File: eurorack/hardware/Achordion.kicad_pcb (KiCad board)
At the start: 4 copper layers, 44.5 x 109.4 mm, 120 parts, among them J1 Power, J10 Jack, J11 Jack, J2 Serial, J3 SWD, J4 Jack, J5 Jack, J6 Jack, J7 Jack, J8 Jack, J9 Jack, SW2 Button, U1 STM32F405RGT6, U10 SC39-11SURKWA, U2 LM1117-3.3, U3 LM1117-3.3, U4 LM4040C10, U5 TLV320AIC23BPW, U6 TL072, U7 MCP6002, U8 MCP6002, U9 MCP6002, Y1 8MHz

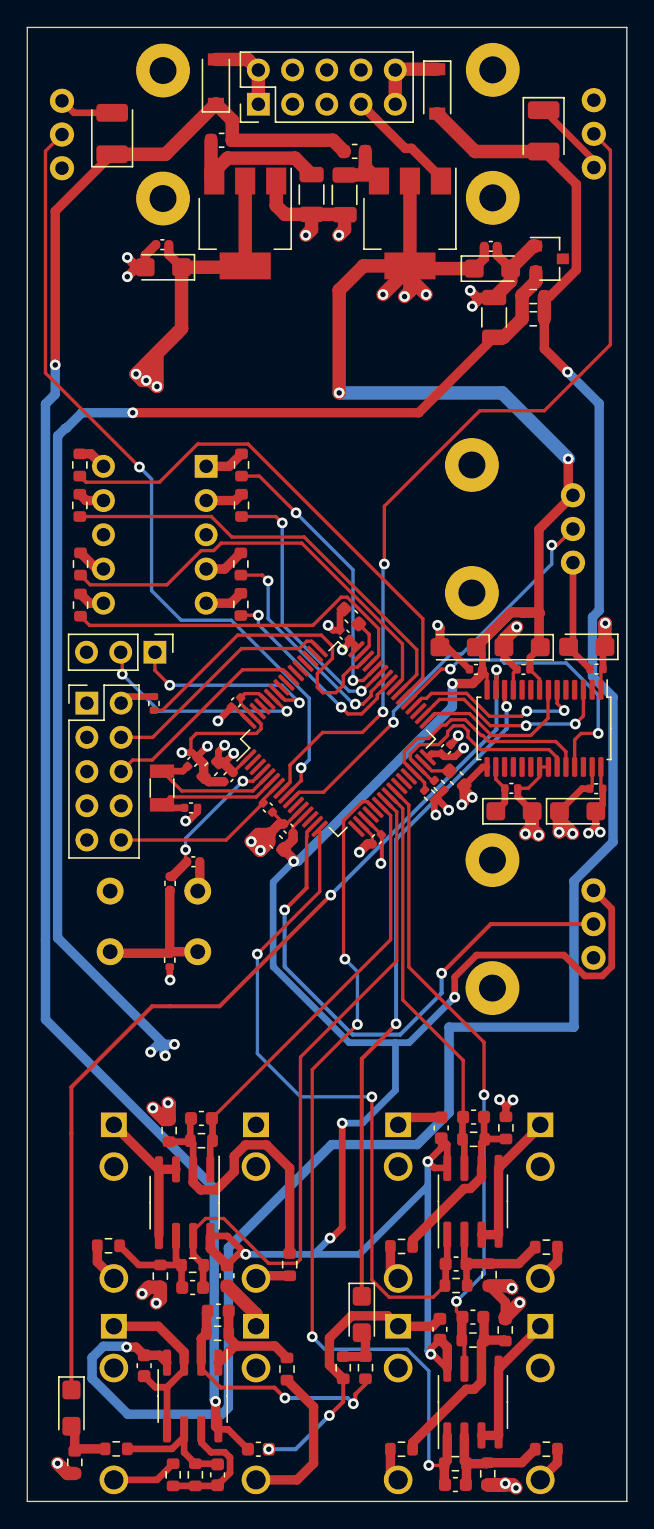
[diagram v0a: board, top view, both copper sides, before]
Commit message: Add labels to PCB
Signed-off-by: Petr Horacek <hrck@protonmail.com>
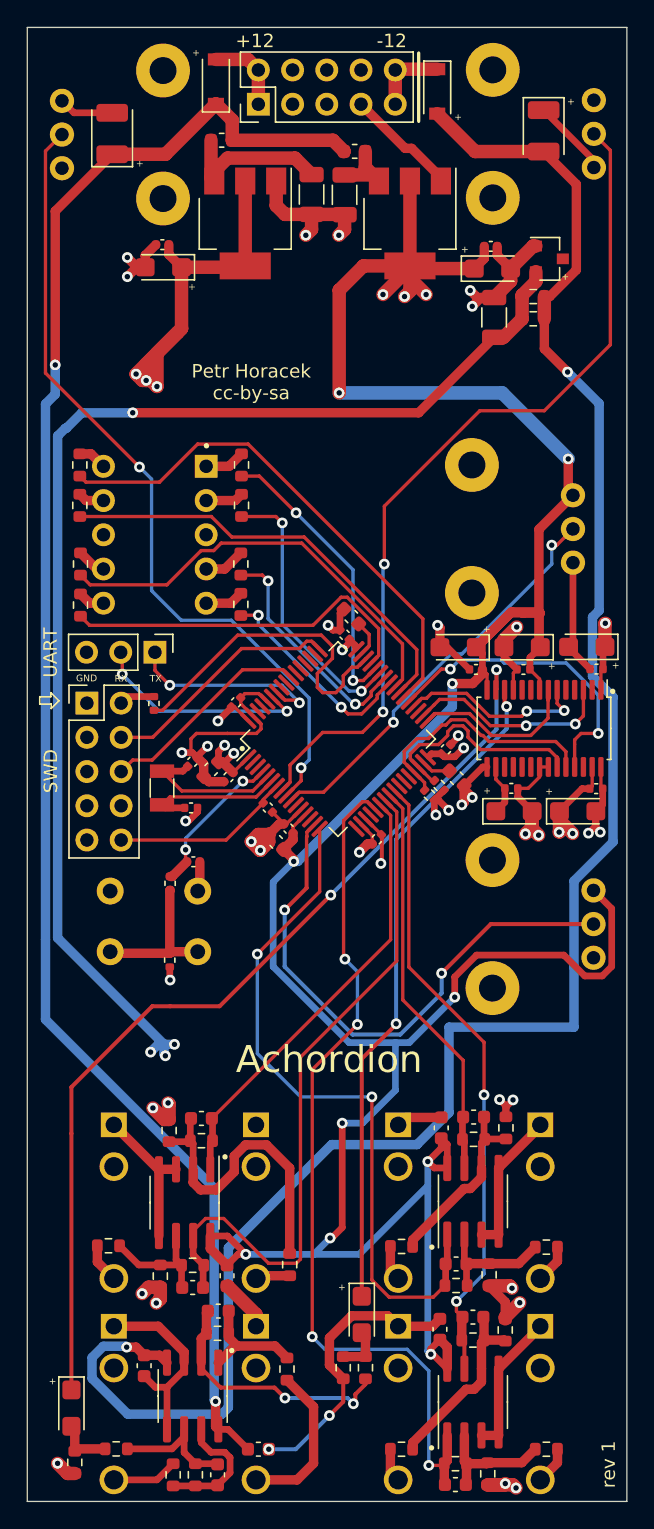
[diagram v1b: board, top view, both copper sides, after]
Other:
- board text added: "+"
- board text added: "+12"
- board text added: "-12"
- board text added: "Achordion"
- board text added: "GND"
- board text added: "Petr Horacek cc-by-sa"
- board text added: "RX"
- board text added: "SWD"
- board text added: "TX"
- board text added: "UART"
- board text added: "rev 1"

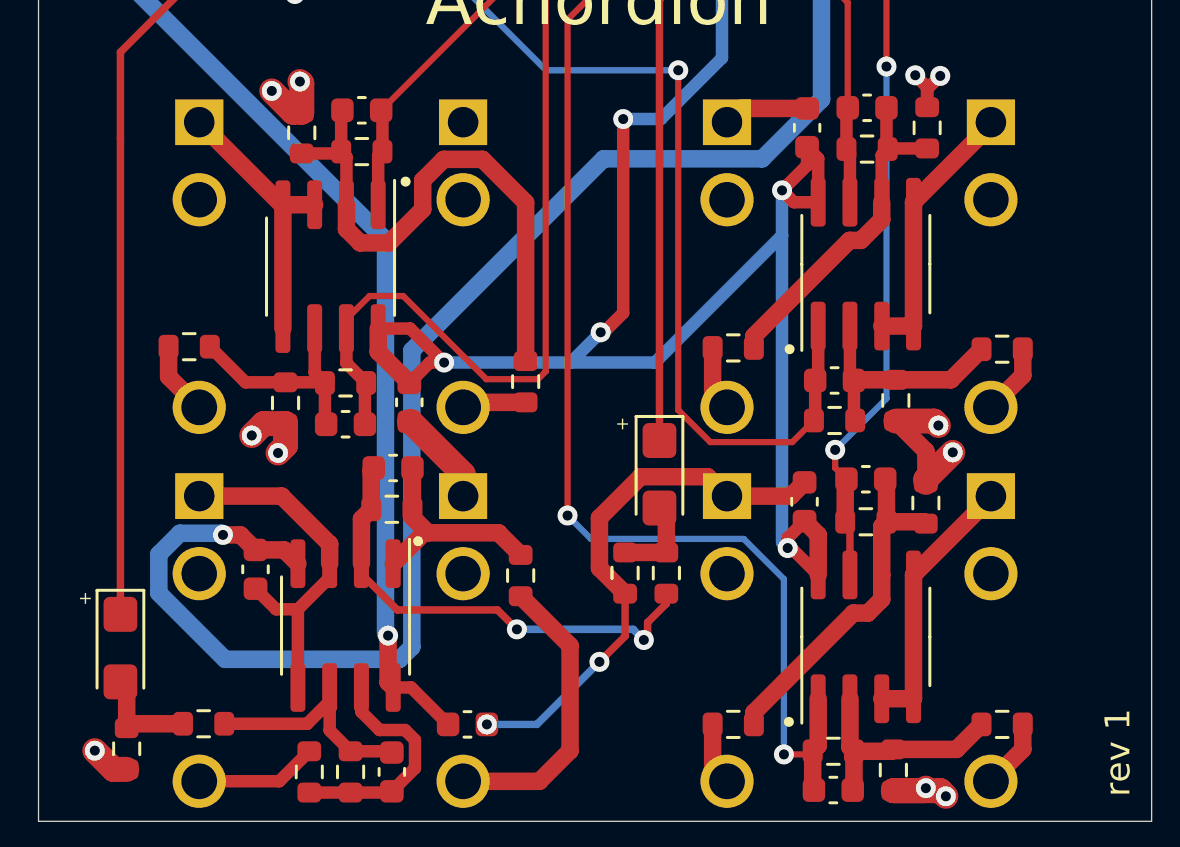
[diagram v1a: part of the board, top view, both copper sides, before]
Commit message: Cut out holes below jacks
Signed-off-by: Petr Horacek <hrck@protonmail.com>
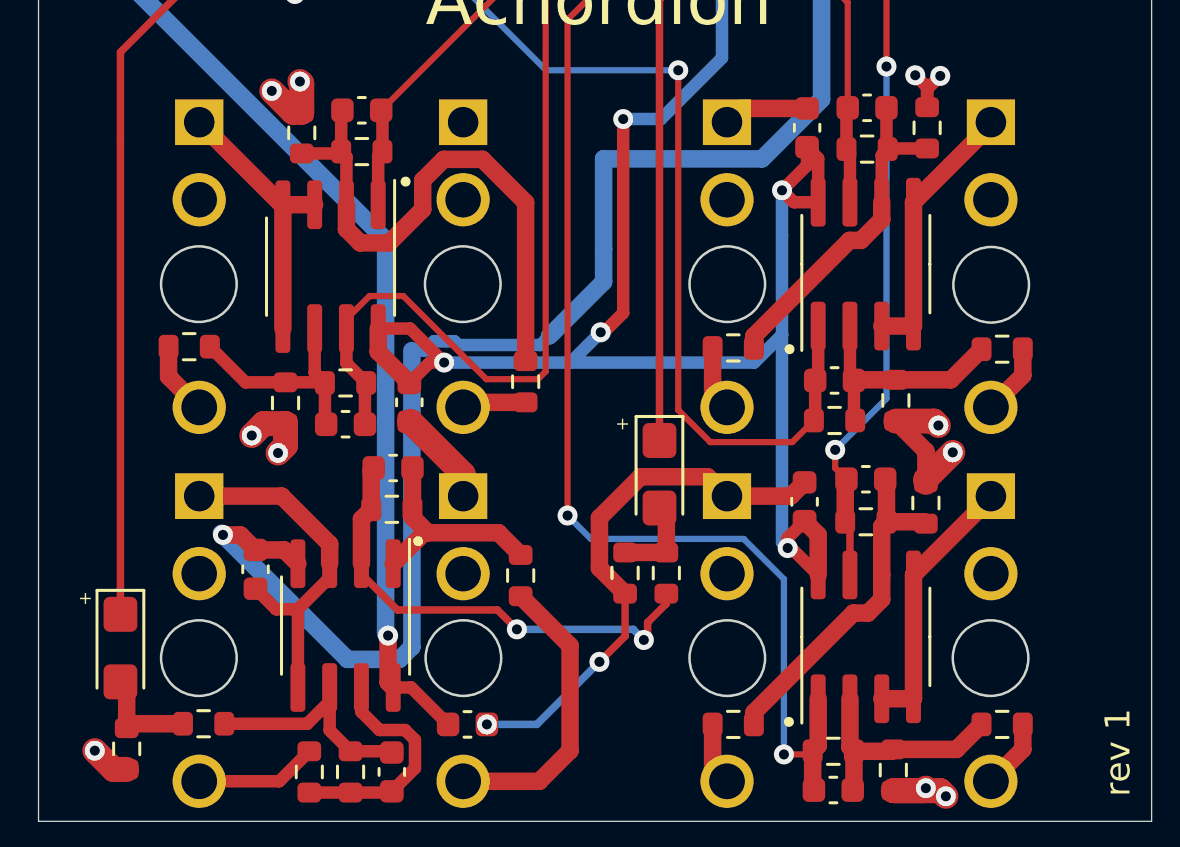
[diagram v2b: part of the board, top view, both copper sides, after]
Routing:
- net VEE: track 147.4 -> 144.4 mm
- net +3.3VA: track 231.3 -> 229.6 mm
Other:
- outline, holes or cut-outs redrawn
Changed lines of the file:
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@@
   (general
     (thickness 1.6)
-    (drawings 43)
-    (tracks 1046)
+    (drawings 51)
+    (tracks 1053)
     (zones 0)
     (modules 120)
@@
     (1 In1.Cu power hide)
     (2 In2.Cu power hide)
-    (31 B.Cu signal hide)
+    (31 B.Cu signal)
     (32 B.Adhes user)
     (33 F.Adhes user)
@@
   )
   (setup
-    (last_trace_width 0.25)
+    (last_trace_width 0.7)
     (user_trace_width 0.3)
     (user_trace_width 0.5)
@@
     )
   )
+  (gr_circle (center 129.236001 144.45) (end 130.747002 144.45) (layer Edge.Cuts) (width 0.1))
+  (gr_circle (center 139.811001 144.45) (end 141.322002 144.45) (layer Edge.Cuts) (width 0.1))
+  (gr_circle (center 150.361001 144.45) (end 151.872002 144.45) (layer Edge.Cuts) (width 0.1))
+  (gr_circle (center 160.886001 144.45) (end 162.397002 144.45) (layer Edge.Cuts) (width 0.1))
+  (gr_circle (center 160.911001 129.525) (end 162.422002 129.525) (layer Edge.Cuts) (width 0.1))
+  (gr_circle (center 150.361001 129.5) (end 151.872002 129.5) (layer Edge.Cuts) (width 0.1))
+  (gr_circle (center 129.236001 129.5) (end 130.747002 129.5) (layer Edge.Cuts) (width 0.1))
+  (gr_circle (center 139.786001 129.5) (end 141.297002 129.5) (layer Edge.Cuts) (width 0.1))
   (gr_text + (at 135.05 60.825) (layer F.SilkS)
     (effects (font (size 0.5 0.5) (thickness 0.125)))
@@
   (segment (start 152.775 140.05) (end 152.92 140.05) (width 0.5) (layer F.Cu) (net 5))
   (via (at 139.040948 132.634052) (size 0.8) (drill 0.4) (layers F.Cu B.Cu) (net 5))
-  (segment (start 152.55 127.55) (end 147.465948 132.634052) (width 0.5) (layer B.Cu) (net 5))
   (segment (start 152.55 125.75) (end 152.55 127.55) (width 0.5) (layer B.Cu) (net 5))
-  (segment (start 152.55 127.55) (end 152.55 139.825) (width 0.5) (layer B.Cu) (net 5))
   (segment (start 138.465948 132.634052) (end 137.65 133.45) (width 0.5) (layer F.Cu) (net 5))
   (segment (start 139.040948 132.634052) (end 138.465948 132.634052) (width 0.5) (layer F.Cu) (net 5))
@@
   (segment (start 143.984052 132.634052) (end 139.040948 132.634052) (width 0.5) (layer B.Cu) (net 5))
   (segment (start 145.3 131.425) (end 144.090948 132.634052) (width 0.5) (layer B.Cu) (net 5))
-  (segment (start 147.465948 132.634052) (end 143.984052 132.634052) (width 0.5) (layer B.Cu) (net 5))
+  (segment (start 151.440948 132.634052) (end 152.55 131.525) (width 0.5) (layer B.Cu) (net 5))
+  (segment (start 143.984052 132.634052) (end 151.440948 132.634052) (width 0.5) (layer B.Cu) (net 5))
+  (segment (start 152.55 131.525) (end 152.55 139.825) (width 0.5) (layer B.Cu) (net 5))
+  (segment (start 152.55 127.55) (end 152.55 131.525) (width 0.5) (layer B.Cu) (net 5))
   (segment (start 134.29096 98.24096) (end 132.825 96.775) (width 0.25) (layer F.Cu) (net 6))
   (segment (start 139.561984 98.24096) (end 134.29096 98.24096) (width 0.25) (layer F.Cu) (net 6))
@@
   (segment (start 163.4 111.321002) (end 163.4 115.775) (width 0.7) (layer B.Cu) (net 11))
   (via (at 130.2 139.525) (size 0.8) (drill 0.4) (layers F.Cu B.Cu) (net 11))
-  (segment (start 127.634999 140.298299) (end 128.474799 139.458499) (width 0.7) (layer B.Cu) (net 11))
   (segment (start 163.4 115.775) (end 154.130057 115.775) (width 0.7) (layer B.Cu) (net 11))
   (segment (start 154.130057 115.775) (end 154.130057 122.114945) (width 0.7) (layer B.Cu) (net 11))
-  (segment (start 128.474799 139.458499) (end 130.133499 139.458499) (width 0.7) (layer B.Cu) (net 11))
   (segment (start 154.130057 122.114945) (end 151.755001 124.490001) (width 0.7) (layer B.Cu) (net 11))
-  (segment (start 145.415056 124.490001) (end 137.750001 132.155056) (width 0.7) (layer B.Cu) (net 11))
   (segment (start 137.750001 132.155056) (end 137.750001 144.006001) (width 0.7) (layer B.Cu) (net 11))
   (segment (start 137.750001 144.006001) (end 137.256001 144.500001) (width 0.7) (layer B.Cu) (net 11))
   (segment (start 130.133499 139.458499) (end 130.2 139.525) (width 0.7) (layer B.Cu) (net 11))
-  (segment (start 137.256001 144.500001) (end 130.286299 144.500001) (width 0.7) (layer B.Cu) (net 11))
   (segment (start 151.755001 124.490001) (end 145.415056 124.490001) (width 0.7) (layer B.Cu) (net 11))
-  (segment (start 130.286299 144.500001) (end 127.634999 141.848701) (width 0.7) (layer B.Cu) (net 11))
-  (segment (start 127.634999 141.848701) (end 127.634999 140.298299) (width 0.7) (layer B.Cu) (net 11))
   (segment (start 130.9 139.525) (end 131.5 140.125) (width 0.7) (layer F.Cu) (net 11))
   (segment (start 130.2 139.525) (end 130.9 139.525) (width 0.7) (layer F.Cu) (net 11))
+  (segment (start 145.415056 124.490001) (end 145.415056 128.109944) (width 0.7) (layer B.Cu) (net 11))
+  (segment (start 145.415056 129.409944) (end 143.25 131.575) (width 0.7) (layer B.Cu) (net 11))
+  (segment (start 145.415056 128.109944) (end 145.415056 129.409944) (width 0.7) (layer B.Cu) (net 11))
+  (segment (start 138.632995 131.784151) (end 139.448901 131.784151) (width 0.5) (layer B.Cu) (net 11))
+  (segment (start 138.26209 132.155056) (end 138.632995 131.784151) (width 0.5) (layer B.Cu) (net 11))
+  (segment (start 137.750001 132.155056) (end 138.26209 132.155056) (width 0.5) (layer B.Cu) (net 11))
+  (segment (start 139.448901 131.784151) (end 139.598892 131.934142) (width 0.5) (layer B.Cu) (net 11))
+  (segment (start 142.890858 131.934142) (end 143.25 131.575) (width 0.5) (layer B.Cu) (net 11))
+  (segment (start 139.598892 131.934142) (end 142.890858 131.934142) (width 0.5) (layer B.Cu) (net 11))
+  (segment (start 137.255901 144.499901) (end 137.256001 144.500001) (width 0.7) (layer B.Cu) (net 11))
+  (segment (start 135.174901 144.499901) (end 137.255901 144.499901) (width 0.7) (layer B.Cu) (net 11))
+  (segment (start 130.2 139.525) (end 135.174901 144.499901) (width 0.7) (layer B.Cu) (net 11))
   (segment (start 158.3 136.175) (end 158.3 137.425) (width 0.7) (layer F.Cu) (net 12))
   (segment (start 157.1 134.975) (end 158.3 136.175) (width 0.7) (layer F.Cu) (net 12))

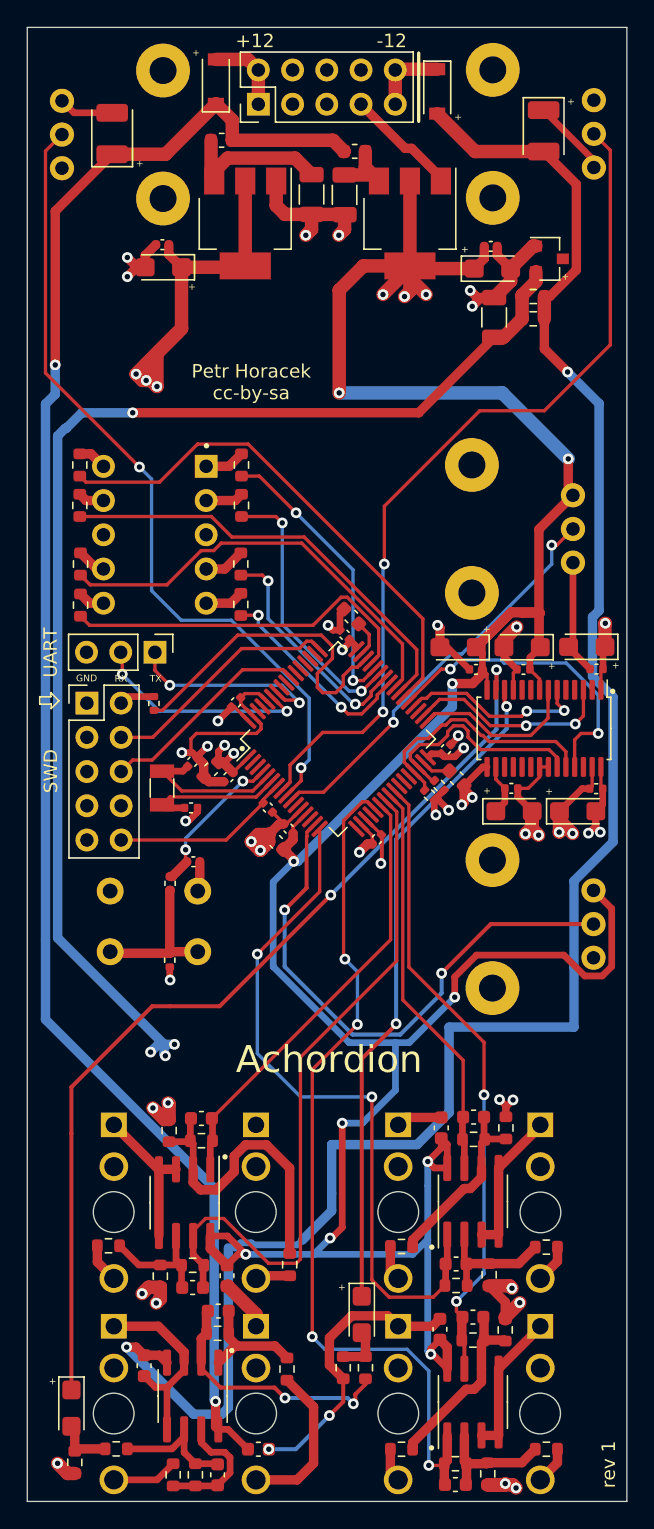
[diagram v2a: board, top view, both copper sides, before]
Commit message: Add mounting holes
Signed-off-by: Petr Horacek <hrck@protonmail.com>
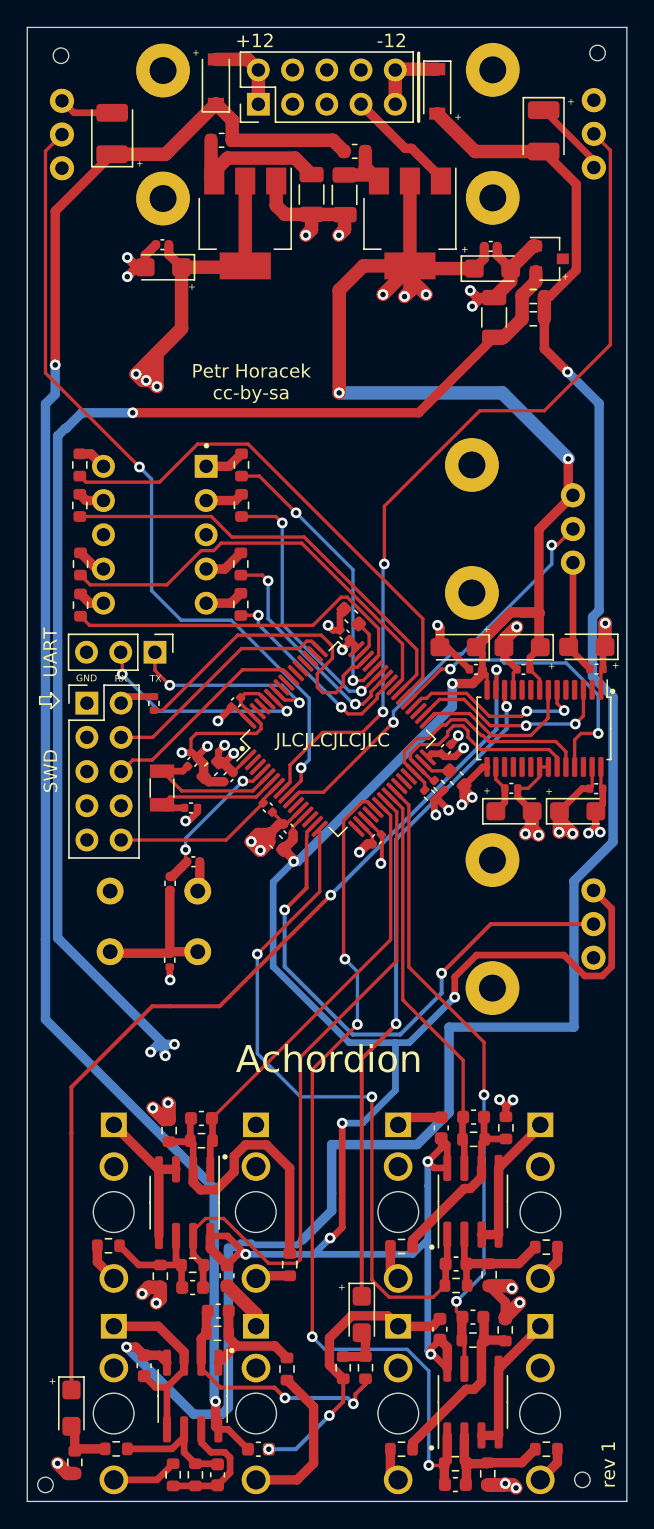
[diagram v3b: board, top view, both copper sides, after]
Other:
- outline, holes or cut-outs redrawn
- board text added: "JLCJLCJLCJLC"
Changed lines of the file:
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@@
   (general
     (thickness 1.6)
-    (drawings 51)
+    (drawings 56)
     (tracks 1053)
     (zones 0)
@@
     )
   )
+  (gr_circle (center 164.025 149.374) (end 164.601 149.374) (layer Edge.Cuts) (width 0.09))
+  (gr_circle (center 124.175 149.749) (end 124.751 149.749) (layer Edge.Cuts) (width 0.09))
+  (gr_circle (center 165.15 43.474) (end 165.726 43.474) (layer Edge.Cuts) (width 0.09))
+  (gr_circle (center 125.325 43.674) (end 125.901 43.674) (layer Edge.Cuts) (width 0.09))
+  (gr_text JLCJLCJLCJLC (at 145.5 94.475) (layer F.SilkS)
+    (effects (font (size 1 1) (thickness 0.15)))
+  )
   (gr_circle (center 129.236001 144.45) (end 130.747002 144.45) (layer Edge.Cuts) (width 0.1))
